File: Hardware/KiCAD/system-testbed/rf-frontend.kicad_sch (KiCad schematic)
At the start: 42 parts

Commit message: feat: assign 0603 passive component footprints #32 #34
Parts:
- C1, C10, C11, C12, C14, C15, C17, C171, C172, C173, C174, C175, C176, C177, C181, C191, C2, C201, C3, C4, C9: footprint Capacitor_SMD:C_0402_1005Metric -> Capacitor_SMD:C_0603_1608Metric
- L1, L171, L172, L173, L174, L18, L191, L192, L193, L2, L201, L3, L5, L7, L8, L9: footprint Inductor_SMD:L_0402_1005Metric -> Inductor_SMD:L_0603_1608Metric
- R171, R2: footprint Resistor_SMD:R_0402_1005Metric -> Resistor_SMD:R_0603_1608Metric
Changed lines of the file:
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@@
 			)
 		)
-		(property "Footprint" "Resistor_SMD:R_0402_1005Metric"
+		(property "Footprint" "Resistor_SMD:R_0603_1608Metric"
 			(at 133.604 128.524 90)
 			(effects
@@
 			)
 		)
-		(property "Footprint" "Capacitor_SMD:C_0402_1005Metric"
+		(property "Footprint" "Capacitor_SMD:C_0603_1608Metric"
 			(at 134.62 68.58 0)
 			(effects
@@
 			)
 		)
-		(property "Footprint" "Inductor_SMD:L_0402_1005Metric"
+		(property "Footprint" "Inductor_SMD:L_0603_1608Metric"
 			(at 154.94 68.58 0)
 			(effects
@@
 			)
 		)
-		(property "Footprint" "Inductor_SMD:L_0402_1005Metric"
+		(property "Footprint" "Inductor_SMD:L_0603_1608Metric"
 			(at 83.82 66.04 0)
 			(effects
@@
 			)
 		)
-		(property "Footprint" "Capacitor_SMD:C_0402_1005Metric"
+		(property "Footprint" "Capacitor_SMD:C_0603_1608Metric"
 			(at 180.34 77.47 0)
 			(effects
@@
 			)
 		)
-		(property "Footprint" "Inductor_SMD:L_0402_1005Metric"
+		(property "Footprint" "Inductor_SMD:L_0603_1608Metric"
 			(at 144.78 144.78 0)
 			(effects
@@
 			)
 		)
-		(property "Footprint" "Capacitor_SMD:C_0402_1005Metric"
+		(property "Footprint" "Capacitor_SMD:C_0603_1608Metric"
 			(at 53.34 142.24 0)
 			(effects
@@
 			)
 		)
-		(property "Footprint" "Capacitor_SMD:C_0402_1005Metric"
+		(property "Footprint" "Capacitor_SMD:C_0603_1608Metric"
 			(at 160.02 63.5 0)
 			(effects
@@
 			)
 		)
-		(property "Footprint" "Inductor_SMD:L_0402_1005Metric"
+		(property "Footprint" "Inductor_SMD:L_0603_1608Metric"
 			(at 154.94 144.78 0)
 			(effects
@@
 			)
 		)
-		(property "Footprint" "Inductor_SMD:L_0402_1005Metric"
+		(property "Footprint" "Inductor_SMD:L_0603_1608Metric"
 			(at 83.82 142.24 0)
 			(effects
@@
 			)
 		)
-		(property "Footprint" "Capacitor_SMD:C_0402_1005Metric"
+		(property "Footprint" "Capacitor_SMD:C_0603_1608Metric"
 			(at 134.62 144.78 0)
 			(effects
@@
 			)
 		)
-		(property "Footprint" "Inductor_SMD:L_0402_1005Metric"
+		(property "Footprint" "Inductor_SMD:L_0603_1608Metric"
 			(at 63.5 142.24 0)
 			(effects
@@
 			)
 		)
-		(property "Footprint" "Inductor_SMD:L_0402_1005Metric"
+		(property "Footprint" "Inductor_SMD:L_0603_1608Metric"
 			(at 129.54 63.5 0)
 			(effects
@@
 			)
 		)
-		(property "Footprint" "Capacitor_SMD:C_0402_1005Metric"
+		(property "Footprint" "Capacitor_SMD:C_0603_1608Metric"
 			(at 124.46 52.07 0)
 			(effects
@@
 			)
 		)
-		(property "Footprint" "Inductor_SMD:L_0402_1005Metric"
+		(property "Footprint" "Inductor_SMD:L_0603_1608Metric"
 			(at 68.58 137.16 0)
 			(effects
@@
 			)
 		)
-		(property "Footprint" "Capacitor_SMD:C_0402_1005Metric"
+		(property "Footprint" "Capacitor_SMD:C_0603_1608Metric"
 			(at 53.34 66.04 0)
 			(effects
@@
 			)
 		)
-		(property "Footprint" "Capacitor_SMD:C_0402_1005Metric"
+		(property "Footprint" "Capacitor_SMD:C_0603_1608Metric"
 			(at 124.46 128.27 0)
 			(effects
@@
 			)
 		)
-		(property "Footprint" "Inductor_SMD:L_0402_1005Metric"
+		(property "Footprint" "Inductor_SMD:L_0603_1608Metric"
 			(at 46.99 157.48 0)
 			(effects
@@
 			)
 		)
-		(property "Footprint" "Capacitor_SMD:C_0402_1005Metric"
+		(property "Footprint" "Capacitor_SMD:C_0603_1608Metric"
 			(at 144.78 153.67 0)
 			(effects
@@
 			)
 		)
-		(property "Footprint" "Resistor_SMD:R_0402_1005Metric"
+		(property "Footprint" "Resistor_SMD:R_0603_1608Metric"
 			(at 133.604 52.324 90)
 			(effects
@@
 			)
 		)
-		(property "Footprint" "Capacitor_SMD:C_0402_1005Metric"
+		(property "Footprint" "Capacitor_SMD:C_0603_1608Metric"
 			(at 109.22 125.73 0)
 			(effects
@@
 			)
 		)
-		(property "Footprint" "Capacitor_SMD:C_0402_1005Metric"
+		(property "Footprint" "Capacitor_SMD:C_0603_1608Metric"
 			(at 109.22 49.53 0)
 			(effects
@@
 			)
 		)
-		(property "Footprint" "Capacitor_SMD:C_0402_1005Metric"
+		(property "Footprint" "Capacitor_SMD:C_0603_1608Metric"
 			(at 144.78 77.47 0)
 			(effects
@@
 			)
 		)
-		(property "Footprint" "Inductor_SMD:L_0402_1005Metric"
+		(property "Footprint" "Inductor_SMD:L_0603_1608Metric"
 			(at 144.78 68.58 0)
 			(effects
@@
 			)
 		)
-		(property "Footprint" "Inductor_SMD:L_0402_1005Metric"
+		(property "Footprint" "Inductor_SMD:L_0603_1608Metric"
 			(at 63.5 66.04 0)
 			(effects
@@
 			)
 		)
-		(property "Footprint" "Capacitor_SMD:C_0402_1005Metric"
+		(property "Footprint" "Capacitor_SMD:C_0603_1608Metric"
 			(at 34.29 157.48 0)
 			(effects
@@
 			)
 		)
-		(property "Footprint" "Capacitor_SMD:C_0402_1005Metric"
+		(property "Footprint" "Capacitor_SMD:C_0603_1608Metric"
 			(at 99.06 125.73 0)
 			(effects
@@
 			)
 		)
-		(property "Footprint" "Capacitor_SMD:C_0402_1005Metric"
+		(property "Footprint" "Capacitor_SMD:C_0603_1608Metric"
 			(at 99.06 49.53 0)
 			(effects
@@
 			)
 		)
-		(property "Footprint" "Capacitor_SMD:C_0402_1005Metric"
+		(property "Footprint" "Capacitor_SMD:C_0603_1608Metric"
 			(at 73.66 142.24 0)
 			(effects
@@
 			)
 		)
-		(property "Footprint" "Inductor_SMD:L_0402_1005Metric"
+		(property "Footprint" "Inductor_SMD:L_0603_1608Metric"
 			(at 180.34 144.78 0)
 			(effects
@@
 			)
 		)
-		(property "Footprint" "Inductor_SMD:L_0402_1005Metric"
+		(property "Footprint" "Inductor_SMD:L_0603_1608Metric"
 			(at 46.99 81.28 0)
 			(effects
@@
 			)
 		)
-		(property "Footprint" "Inductor_SMD:L_0402_1005Metric"
+		(property "Footprint" "Inductor_SMD:L_0603_1608Metric"
 			(at 129.54 139.7 0)
 			(effects
@@
 			)
 		)
-		(property "Footprint" "Inductor_SMD:L_0402_1005Metric"
+		(property "Footprint" "Inductor_SMD:L_0603_1608Metric"
 			(at 180.34 68.58 0)
 			(effects
@@
 			)
 		)
-		(property "Footprint" "Capacitor_SMD:C_0402_1005Metric"
+		(property "Footprint" "Capacitor_SMD:C_0603_1608Metric"
 			(at 165.1 149.86 0)
 			(effects
@@
 			)
 		)
-		(property "Footprint" "Inductor_SMD:L_0402_1005Metric"
+		(property "Footprint" "Inductor_SMD:L_0603_1608Metric"
 			(at 68.58 60.96 0)
 			(effects
@@
 			)
 		)
-		(property "Footprint" "Capacitor_SMD:C_0402_1005Metric"
+		(property "Footprint" "Capacitor_SMD:C_0603_1608Metric"
 			(at 165.1 73.66 0)
 			(effects
@@
 			)
 		)
-		(property "Footprint" "Capacitor_SMD:C_0402_1005Metric"
+		(property "Footprint" "Capacitor_SMD:C_0603_1608Metric"
 			(at 160.02 139.7 0)
 			(effects
@@
 			)
 		)
-		(property "Footprint" "Capacitor_SMD:C_0402_1005Metric"
+		(property "Footprint" "Capacitor_SMD:C_0603_1608Metric"
 			(at 34.29 81.28 0)
 			(effects
@@
 			)
 		)
-		(property "Footprint" "Capacitor_SMD:C_0402_1005Metric"
+		(property "Footprint" "Capacitor_SMD:C_0603_1608Metric"
 			(at 73.66 66.04 0)
 			(effects

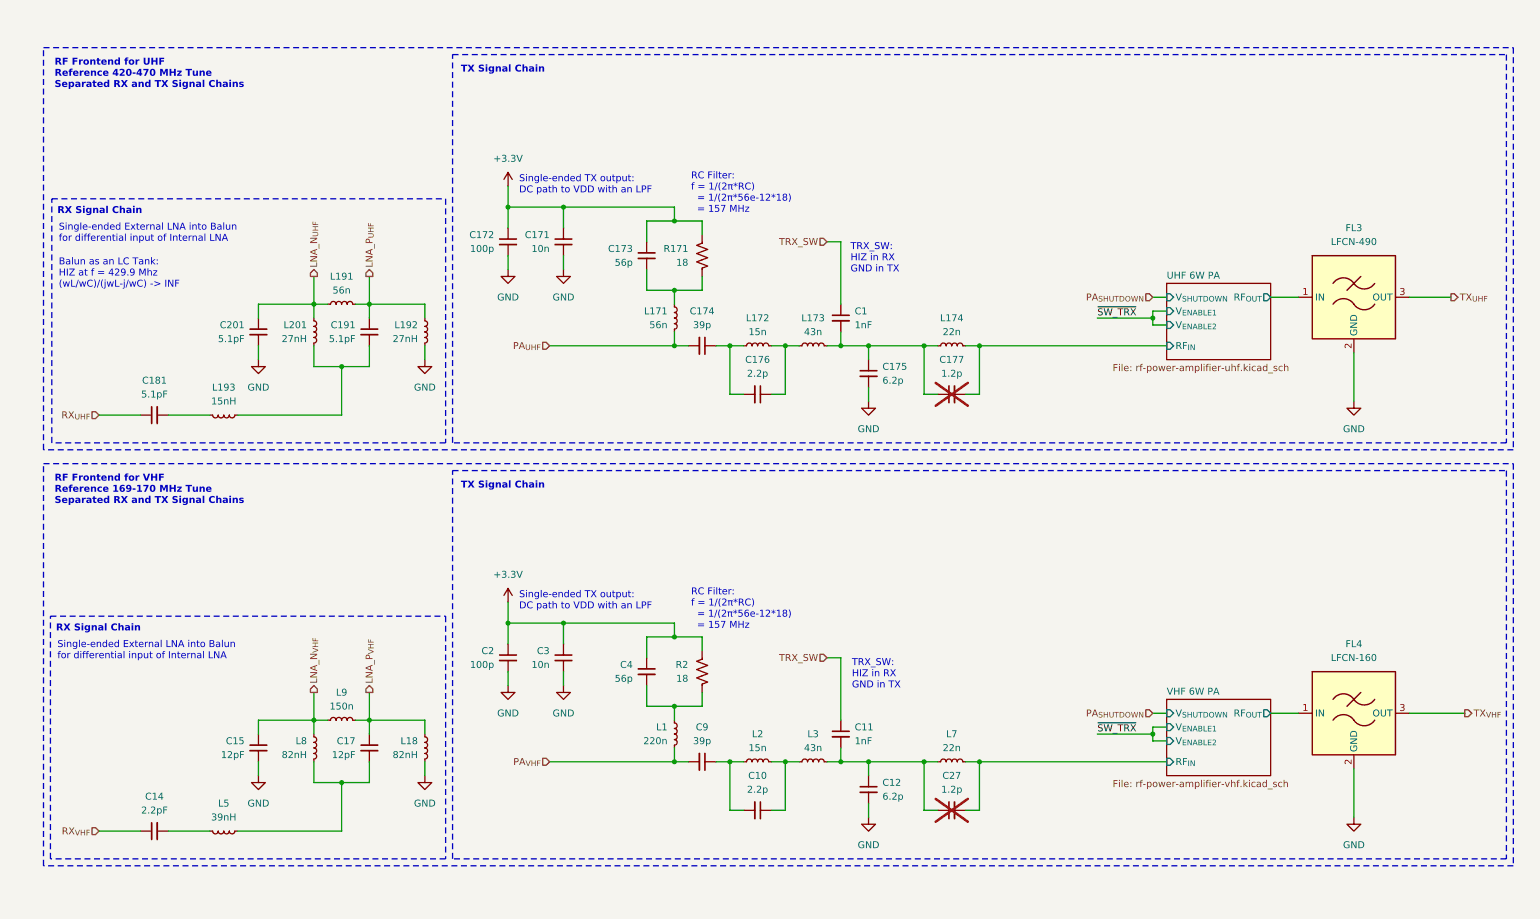
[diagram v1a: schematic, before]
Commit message: fix: import RF sheet contents #65
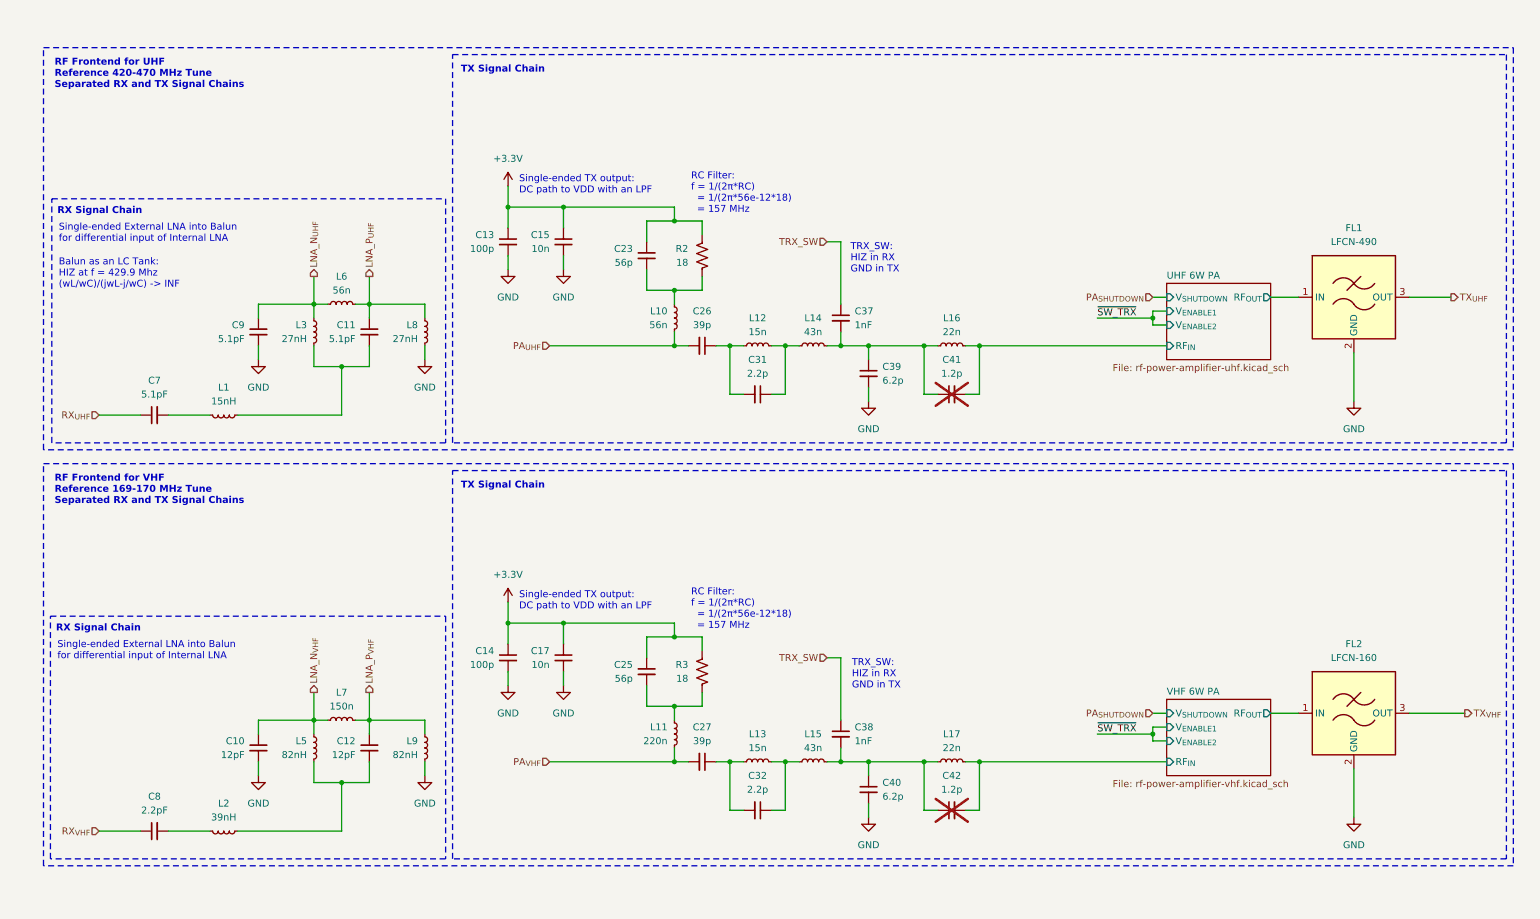
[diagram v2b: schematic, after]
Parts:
- renumbered C15 to C10, C191 to C11, C17 to C12, C172 to C13, C2 to C14, C171 to C15, C3 to C17, C173 to C23, C4 to C25, C174 to C26, C9 to C27, C176 to C31, C10 to C32, C1 to C37, C11 to C38, C175 to C39, C12 to C40, C177 to C41, C27 to C42, C181 to C7, C14 to C8, C201 to C9, FL3 to FL1, FL4 to FL2, L193 to L1, L171 to L10, L1 to L11, L172 to L12, L2 to L13, L173 to L14, L3 to L15, L174 to L16, L7 to L17, L5 to L2, L201 to L3, L8 to L5, L191 to L6, L9 to L7, L192 to L8, L18 to L9, R171 to R2, R2 to R3

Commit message: fix: reannotate schematics for pcb editor use #55
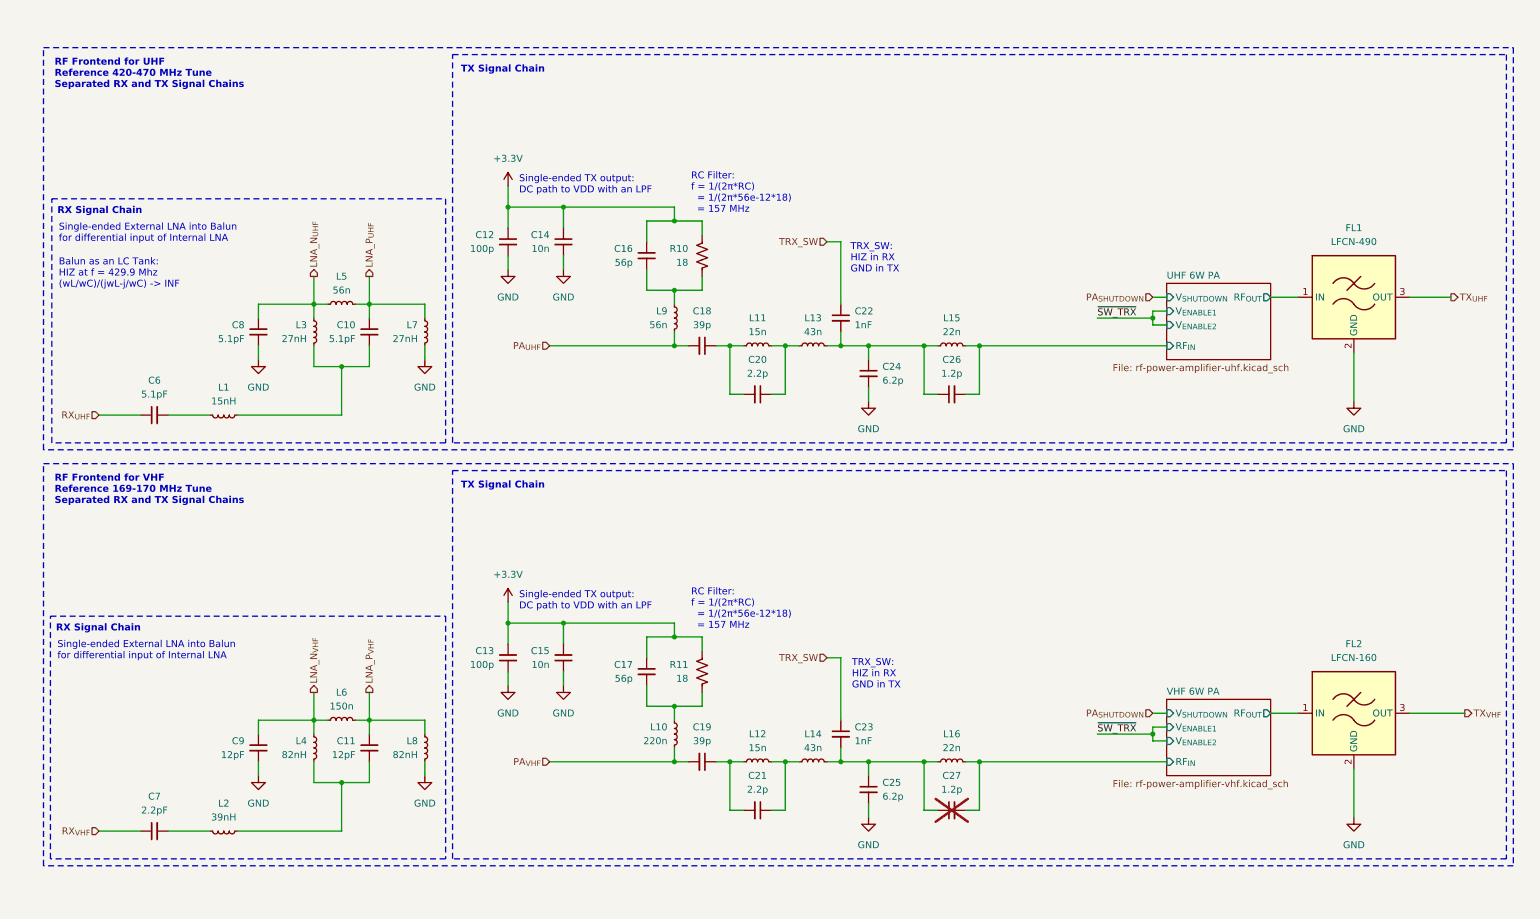
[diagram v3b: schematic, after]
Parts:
- C10: renamed from C11; footprint Capacitor_SMD:C_0603_1608Metric -> Capacitor_SMD:C_0402_1005Metric
- C11: renamed from C12; footprint Capacitor_SMD:C_0603_1608Metric -> Capacitor_SMD:C_0402_1005Metric
- C12: renamed from C13; footprint Capacitor_SMD:C_0603_1608Metric -> Capacitor_SMD:C_0402_1005Metric
- C13: renamed from C14; footprint Capacitor_SMD:C_0603_1608Metric -> Capacitor_SMD:C_0402_1005Metric
- C14: renamed from C15; footprint Capacitor_SMD:C_0603_1608Metric -> Capacitor_SMD:C_0402_1005Metric
- C15: renamed from C17; footprint Capacitor_SMD:C_0603_1608Metric -> Capacitor_SMD:C_0402_1005Metric
- C16: renamed from C23; footprint Capacitor_SMD:C_0603_1608Metric -> Capacitor_SMD:C_0402_1005Metric
- C17: renamed from C25; footprint Capacitor_SMD:C_0603_1608Metric -> Capacitor_SMD:C_0402_1005Metric
- C18: renamed from C26; footprint Capacitor_SMD:C_0603_1608Metric -> Capacitor_SMD:C_0402_1005Metric
- C19: renamed from C27; footprint Capacitor_SMD:C_0603_1608Metric -> Capacitor_SMD:C_0402_1005Metric
- C20: renamed from C31; footprint Capacitor_SMD:C_0603_1608Metric -> Capacitor_SMD:C_0402_1005Metric
- C21: renamed from C32; footprint Capacitor_SMD:C_0603_1608Metric -> Capacitor_SMD:C_0402_1005Metric
- C22: renamed from C37; footprint Capacitor_SMD:C_0603_1608Metric -> Capacitor_SMD:C_0402_1005Metric
- C23: renamed from C38; footprint Capacitor_SMD:C_0603_1608Metric -> Capacitor_SMD:C_0402_1005Metric
- C24: renamed from C39; footprint Capacitor_SMD:C_0603_1608Metric -> Capacitor_SMD:C_0402_1005Metric
- C25: renamed from C40; footprint Capacitor_SMD:C_0603_1608Metric -> Capacitor_SMD:C_0402_1005Metric
- C26: renamed from C41; footprint Capacitor_SMD:C_0603_1608Metric -> Capacitor_SMD:C_0402_1005Metric; now fitted
- C6: renamed from C7; footprint Capacitor_SMD:C_0603_1608Metric -> Capacitor_SMD:C_0402_1005Metric
- C7: renamed from C8; footprint Capacitor_SMD:C_0603_1608Metric -> Capacitor_SMD:C_0402_1005Metric
- C8: renamed from C9; footprint Capacitor_SMD:C_0603_1608Metric -> Capacitor_SMD:C_0402_1005Metric
- C9: renamed from C10; footprint Capacitor_SMD:C_0603_1608Metric -> Capacitor_SMD:C_0402_1005Metric
- L1, L2, L3: footprint Inductor_SMD:L_0603_1608Metric -> Inductor_SMD:L_0402_1005Metric
- L10: renamed from L11; footprint Inductor_SMD:L_0603_1608Metric -> Capacitor_SMD:C_0402_1005Metric
- L11: renamed from L12; footprint Inductor_SMD:L_0603_1608Metric -> Inductor_SMD:L_0402_1005Metric
- L12: renamed from L13; footprint Inductor_SMD:L_0603_1608Metric -> Inductor_SMD:L_0402_1005Metric
- L13: renamed from L14; footprint Inductor_SMD:L_0603_1608Metric -> Inductor_SMD:L_0402_1005Metric
- L14: renamed from L15; footprint Inductor_SMD:L_0603_1608Metric -> Inductor_SMD:L_0402_1005Metric
- L15: renamed from L16; footprint Inductor_SMD:L_0603_1608Metric -> Inductor_SMD:L_0402_1005Metric
- L16: renamed from L17; footprint Inductor_SMD:L_0603_1608Metric -> Inductor_SMD:L_0402_1005Metric
- L4: renamed from L5; footprint Inductor_SMD:L_0603_1608Metric -> Inductor_SMD:L_0402_1005Metric
- L5: renamed from L6; footprint Inductor_SMD:L_0603_1608Metric -> Inductor_SMD:L_0402_1005Metric
- L6: renamed from L7; footprint Inductor_SMD:L_0603_1608Metric -> Inductor_SMD:L_0402_1005Metric
- L7: renamed from L8; footprint Inductor_SMD:L_0603_1608Metric -> Inductor_SMD:L_0402_1005Metric
- L8: renamed from L9; footprint Inductor_SMD:L_0603_1608Metric -> Inductor_SMD:L_0402_1005Metric
- L9: renamed from L10; footprint Inductor_SMD:L_0603_1608Metric -> Inductor_SMD:L_0402_1005Metric
- R10: renamed from R2; footprint Resistor_SMD:R_0603_1608Metric -> Resistor_SMD:R_0402_1005Metric
- R11: renamed from R3; footprint Resistor_SMD:R_0603_1608Metric -> Resistor_SMD:R_0402_1005Metric
- renumbered C42 to C27

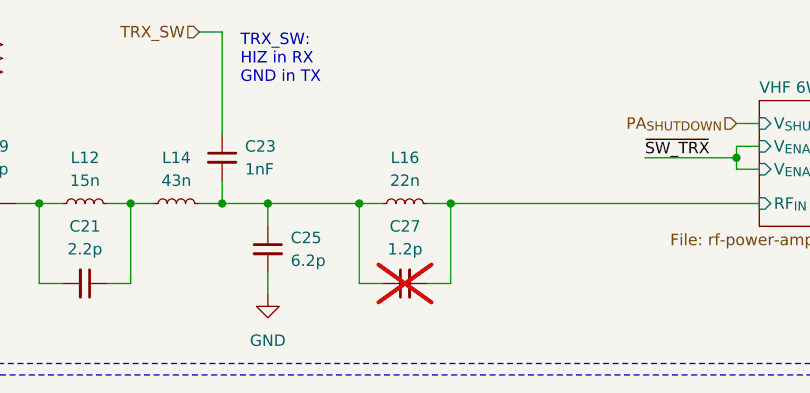
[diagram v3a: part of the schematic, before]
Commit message: fix: allow for DRC use in PCB editor by successful reannotation
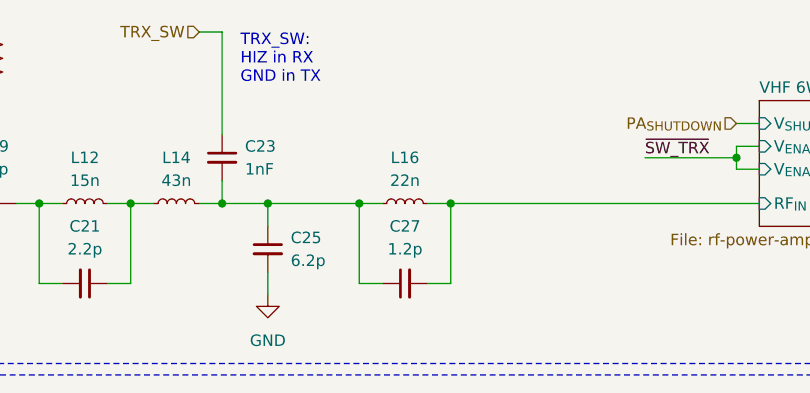
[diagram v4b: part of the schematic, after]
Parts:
- C27: now fitted
- C6: footprint Capacitor_SMD:C_0402_1005Metric -> Capacitor_SMD:C_0603_1608Metric
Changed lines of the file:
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@@
 		(in_bom yes)
 		(on_board yes)
-		(dnp yes)
+		(dnp no)
 		(fields_autoplaced yes)
 		(property "Reference" "C27"
@@
 			)
 		)
-		(property "Datasheet" "~"
+		(property "Datasheet" ""
 			(at 180.34 153.67 0)
 			(effects
@@
 			)
 		)
-		(property "Description" "Unpolarized capacitor, small symbol"
+		(property "Description" ""
 			(at 180.34 153.67 0)
 			(effects
@@
 			)
 		)
-		(property "Datasheet" "~"
+		(property "Datasheet" ""
 			(at 129.54 139.7 0)
 			(effects
@@
 			)
 		)
-		(property "Footprint" "Capacitor_SMD:C_0402_1005Metric"
+		(property "Footprint" "Capacitor_SMD:C_0603_1608Metric"
 			(at 34.29 81.28 0)
 			(effects
